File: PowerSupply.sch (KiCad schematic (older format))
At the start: 62 parts, among them J1 Conn_01x03, J2 Conn_01x02, J22 Jack-DC, J23 Conn_01x02, J24 Conn_01x02, J25 Conn_01x01, J26 Conn_01x01, J27 Conn_01x01, J28 Conn_01x01, J3 Conn_01x02, J6 Conn_01x01, J7 Conn_01x01, J8 Conn_01x01, J9 Conn_01x01, Q1 2N3904, Q2 TIP42C, U1 LM317, U2 LM337

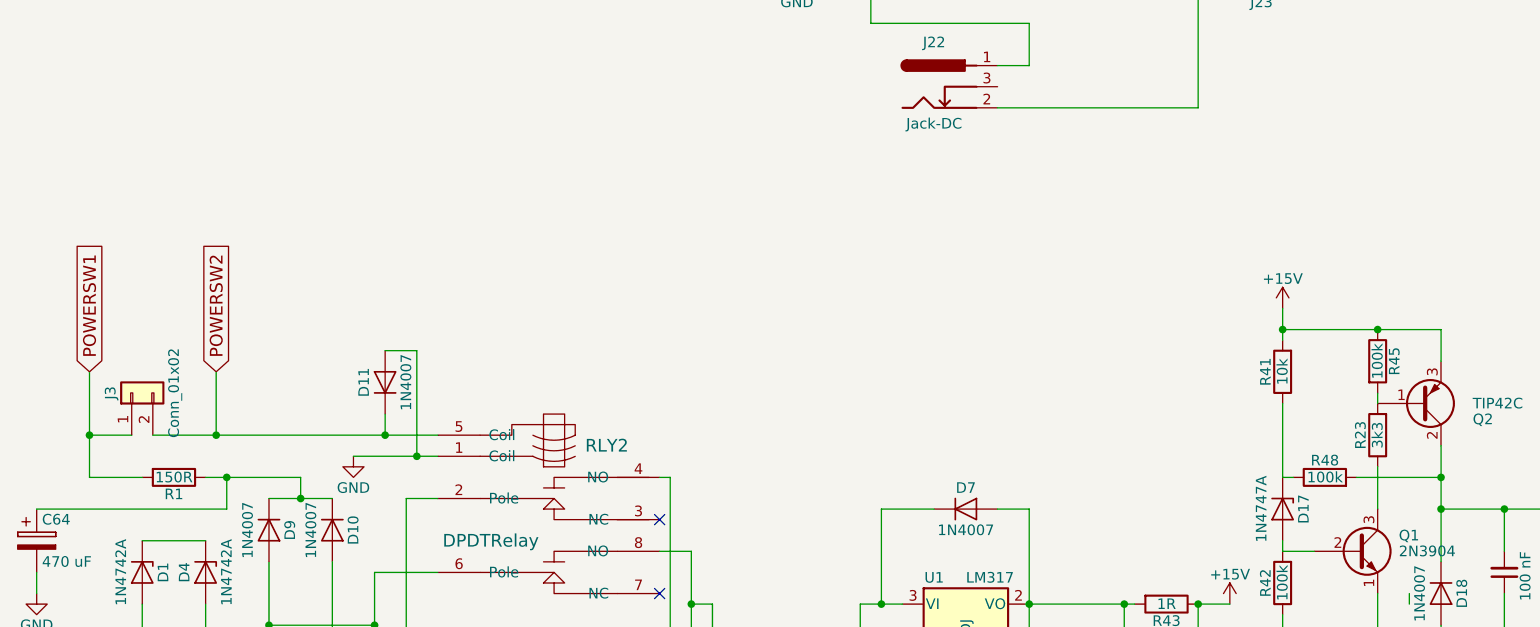
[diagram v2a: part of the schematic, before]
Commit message: Added jumpers to connect shields of XLR to ground
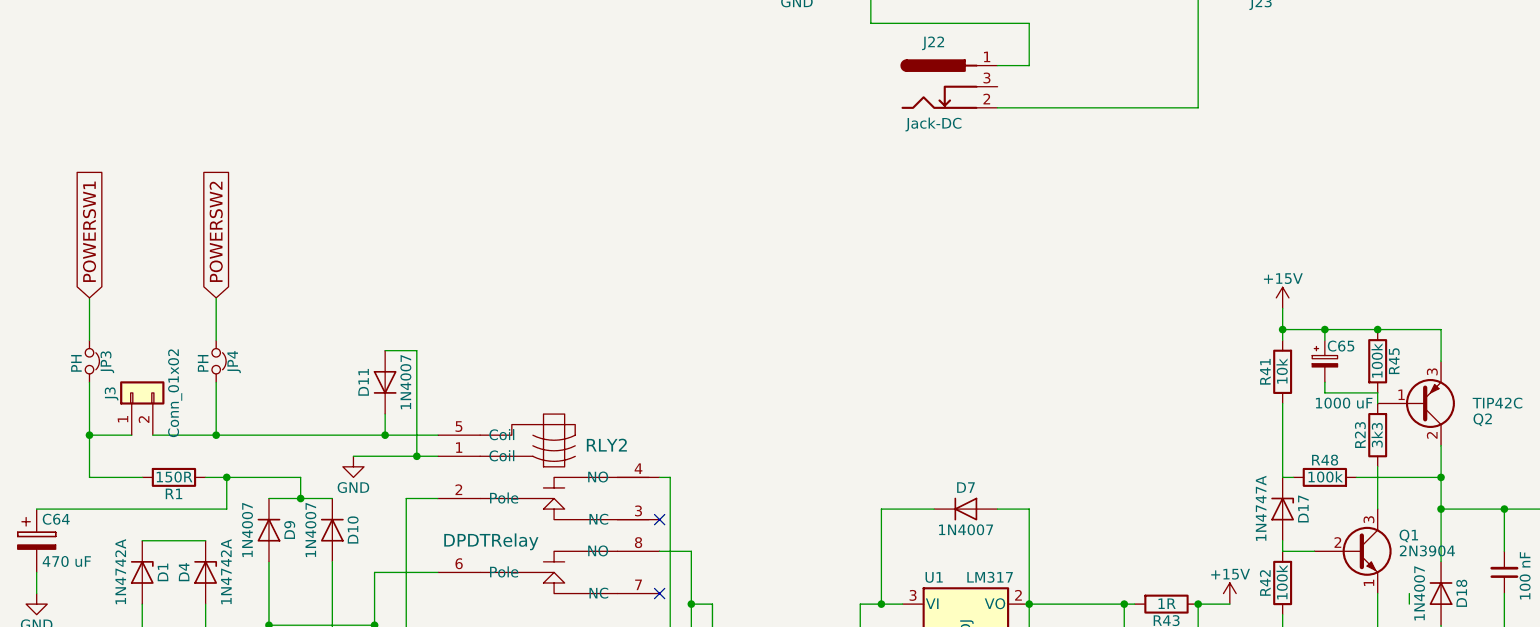
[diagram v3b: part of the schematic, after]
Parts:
- added C65: 1000 uF, Capacitors_THT:CP_Radial_D7.5mm_P2.50mm, symbol CP_Small
- added JP3, JP4: PH, Pin_Headers:Pin_Header_Straight_1x02_Pitch2.54mm, symbol Jumper_NC_Small
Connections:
- net +15V: now also C65.1
- net POWERSW1: now also JP3.1; no longer J3.1 (Pin_1), R1.2
- net POWERSW2: now also JP4.1; no longer D11.1 (K), J3.2 (Pin_2), RLY2.5 (Coil)
- net at Q2.1 (B), R23.2, R45.2: now also C65.2
- new net: D11.1 (K), J3.2 (Pin_2), JP4.2, RLY2.5 (Coil)
- new net: J3.1 (Pin_1), JP3.2, R1.2
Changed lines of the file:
@@
 $EndComp
 $Comp
-L GND #PWR81
+L GND #PWR83
 U 1 1 606D5FED
 P 1350 7050
-F 0 "#PWR81" H 1350 6800 50  0001 C CNN
+F 0 "#PWR83" H 1350 6800 50  0001 C CNN
 F 1 "GND" H 1350 6900 50  0000 C CNN
 F 2 "" H 1350 7050 50  0001 C CNN
@@
 $EndComp
 $Comp
-L GND #PWR82
+L GND #PWR84
 U 1 1 606D606A
 P 2150 4900
-F 0 "#PWR82" H 2150 4650 50  0001 C CNN
+F 0 "#PWR84" H 2150 4650 50  0001 C CNN
 F 1 "GND" H 2150 4750 50  0000 C CNN
 F 2 "" H 2150 4900 50  0001 C CNN
@@
 $EndComp
 $Comp
-L GND #PWR84
+L GND #PWR86
 U 1 1 606D6085
 P 4000 7200
-F 0 "#PWR84" H 4000 6950 50  0001 C CNN
+F 0 "#PWR86" H 4000 6950 50  0001 C CNN
 F 1 "GND" H 4000 7050 50  0000 C CNN
 F 2 "" H 4000 7200 50  0001 C CNN
@@
 NoConn ~ 3600 5200
 $Comp
-L GND #PWR89
+L GND #PWR91
 U 1 1 606D60BA
 P 6300 6300
-F 0 "#PWR89" H 6300 6050 50  0001 C CNN
+F 0 "#PWR91" H 6300 6050 50  0001 C CNN
 F 1 "GND" H 6300 6150 50  0000 C CNN
 F 2 "" H 6300 6300 50  0001 C CNN
@@
 	1    0    0    -1
 $EndComp
-Text GLabel 900  4500 1    60   Input ~ 0
+Text GLabel 900  4150 1    60   Input ~ 0
 POWERSW1
-Text GLabel 1500 4500 1    60   Input ~ 0
+Text GLabel 1500 4150 1    60   Input ~ 0
 POWERSW2
 $Comp
@@
 Power Supply
 $Comp
-L GND #PWR93
+L GND #PWR95
 U 1 1 606DF2B7
 P 7300 5750
-F 0 "#PWR93" H 7300 5500 50  0001 C CNN
+F 0 "#PWR95" H 7300 5500 50  0001 C CNN
 F 1 "GND" H 7300 5600 50  0000 C CNN
 F 2 "" H 7300 5750 50  0001 C CNN
@@
 SUBUNBAL
 $Comp
-L GND #PWR104
+L GND #PWR106
 U 1 1 606F678E
 P 10600 1400
-F 0 "#PWR104" H 10600 1150 50  0001 C CNN
+F 0 "#PWR106" H 10600 1150 50  0001 C CNN
 F 1 "GND" H 10600 1250 50  0000 C CNN
 F 2 "" H 10600 1400 50  0001 C CNN
@@
 $EndComp
 $Comp
-L GND #PWR105
+L GND #PWR107
 U 1 1 606F6A81
 P 10600 1750
-F 0 "#PWR105" H 10600 1500 50  0001 C CNN
+F 0 "#PWR107" H 10600 1500 50  0001 C CNN
 F 1 "GND" H 10600 1600 50  0000 C CNN
 F 2 "" H 10600 1750 50  0001 C CNN
@@
 $EndComp
 $Comp
-L GND #PWR97
+L GND #PWR99
 U 1 1 606F6F41
 P 9350 1100
-F 0 "#PWR97" H 9350 850 50  0001 C CNN
+F 0 "#PWR99" H 9350 850 50  0001 C CNN
 F 1 "GND" H 9350 950 50  0000 C CNN
 F 2 "" H 9350 1100 50  0001 C CNN
@@
 $EndComp
 $Comp
-L GND #PWR106
+L GND #PWR108
 U 1 1 606F7436
 P 10600 2450
-F 0 "#PWR106" H 10600 2200 50  0001 C CNN
+F 0 "#PWR108" H 10600 2200 50  0001 C CNN
 F 1 "GND" H 10600 2300 50  0000 C CNN
 F 2 "" H 10600 2450 50  0001 C CNN
@@
 $EndComp
 $Comp
-L GND #PWR107
+L GND #PWR109
 U 1 1 606F7669
 P 10600 2800
-F 0 "#PWR107" H 10600 2550 50  0001 C CNN
+F 0 "#PWR109" H 10600 2550 50  0001 C CNN
 F 1 "GND" H 10600 2650 50  0000 C CNN
 F 2 "" H 10600 2800 50  0001 C CNN
@@
 $EndComp
 $Comp
-L GND #PWR108
+L GND #PWR110
 U 1 1 606F84BF
 P 10600 3450
-F 0 "#PWR108" H 10600 3200 50  0001 C CNN
+F 0 "#PWR110" H 10600 3200 50  0001 C CNN
 F 1 "GND" H 10600 3300 50  0000 C CNN
 F 2 "" H 10600 3450 50  0001 C CNN
@@
 $EndComp
 $Comp
-L GND #PWR109
+L GND #PWR111
 U 1 1 606F8632
 P 10600 3800
-F 0 "#PWR109" H 10600 3550 50  0001 C CNN
+F 0 "#PWR111" H 10600 3550 50  0001 C CNN
 F 1 "GND" H 10600 3650 50  0000 C CNN
 F 2 "" H 10600 3800 50  0001 C CNN
@@
 $EndComp
 $Comp
-L GND #PWR100
+L GND #PWR102
 U 1 1 606F8F91
 P 10550 4450
-F 0 "#PWR100" H 10550 4200 50  0001 C CNN
+F 0 "#PWR102" H 10550 4200 50  0001 C CNN
 F 1 "GND" H 10550 4300 50  0000 C CNN
 F 2 "" H 10550 4450 50  0001 C CNN
@@
 $EndComp
 $Comp
-L GND #PWR101
+L GND #PWR103
 U 1 1 606F910C
 P 10550 4800
-F 0 "#PWR101" H 10550 4550 50  0001 C CNN
+F 0 "#PWR103" H 10550 4550 50  0001 C CNN
 F 1 "GND" H 10550 4650 50  0000 C CNN
 F 2 "" H 10550 4800 50  0001 C CNN
@@
 $EndComp
 $Comp
-L GND #PWR98
+L GND #PWR100
 U 1 1 606F9F16
 P 9350 2150
-F 0 "#PWR98" H 9350 1900 50  0001 C CNN
+F 0 "#PWR100" H 9350 1900 50  0001 C CNN
 F 1 "GND" H 9350 2000 50  0000 C CNN
 F 2 "" H 9350 2150 50  0001 C CNN
@@
 $EndComp
 $Comp
-L GND #PWR99
+L GND #PWR101
 U 1 1 606FA0A1
 P 9350 3150
-F 0 "#PWR99" H 9350 2900 50  0001 C CNN
+F 0 "#PWR101" H 9350 2900 50  0001 C CNN
 F 1 "GND" H 9350 3000 50  0000 C CNN
 F 2 "" H 9350 3150 50  0001 C CNN
@@
 $EndComp
 $Comp
-L GND #PWR96
+L GND #PWR98
 U 1 1 606FA305
 P 9300 4150
-F 0 "#PWR96" H 9300 3900 50  0001 C CNN
+F 0 "#PWR98" H 9300 3900 50  0001 C CNN
 F 1 "GND" H 9300 4000 50  0000 C CNN
 F 2 "" H 9300 4150 50  0001 C CNN
@@
 $EndComp
 $Comp
-L GND #PWR102
+L GND #PWR104
 U 1 1 606FAB7E
 P 10550 5450
-F 0 "#PWR102" H 10550 5200 50  0001 C CNN
+F 0 "#PWR104" H 10550 5200 50  0001 C CNN
 F 1 "GND" H 10550 5300 50  0000 C CNN
 F 2 "" H 10550 5450 50  0001 C CNN
@@
 $EndComp
 $Comp
-L GND #PWR103
+L GND #PWR105
 U 1 1 606FAD7D
 P 10550 5800
-F 0 "#PWR103" H 10550 5550 50  0001 C CNN
+F 0 "#PWR105" H 10550 5550 50  0001 C CNN
 F 1 "GND" H 10550 5650 50  0000 C CNN
 F 2 "" H 10550 5800 50  0001 C CNN
@@
 $EndComp
 $Comp
-L GND #PWR87
+L GND #PWR89
 U 1 1 606FCAFD
 P 4400 2050
-F 0 "#PWR87" H 4400 1800 50  0001 C CNN
+F 0 "#PWR89" H 4400 1800 50  0001 C CNN
 F 1 "GND" H 4400 1900 50  0000 C CNN
 F 2 "" H 4400 2050 50  0001 C CNN
@@
 $EndComp
 $Comp
-L +15V #PWR88
+L +15V #PWR90
 U 1 1 6070415B
 P 6300 5600
-F 0 "#PWR88" H 6300 5450 50  0001 C CNN
+F 0 "#PWR90" H 6300 5450 50  0001 C CNN
 F 1 "+15V" H 6300 5740 50  0000 C CNN
 F 2 "" H 6300 5600 50  0001 C CNN
@@
 $EndComp
 $Comp
-L -15V #PWR90
+L -15V #PWR92
 U 1 1 60704F1D
 P 6300 7000
-F 0 "#PWR90" H 6300 7100 50  0001 C CNN
+F 0 "#PWR92" H 6300 7100 50  0001 C CNN
 F 1 "-15V" H 6300 7150 50  0000 C CNN
 F 2 "" H 6300 7000 50  0001 C CNN
@@
 $EndComp
 $Comp
-L -15V #PWR92
+L -15V #PWR94
 U 1 1 607050A0
 P 6550 5850
-F 0 "#PWR92" H 6550 5950 50  0001 C CNN
+F 0 "#PWR94" H 6550 5950 50  0001 C CNN
 F 1 "-15V" H 6550 6000 50  0000 C CNN
 F 2 "" H 6550 5850 50  0001 C CNN
@@
 $EndComp
 $Comp
-L +15V #PWR91
+L +15V #PWR93
 U 1 1 60705366
 P 6550 4200
-F 0 "#PWR91" H 6550 4050 50  0001 C CNN
+F 0 "#PWR93" H 6550 4050 50  0001 C CNN
 F 1 "+15V" H 6550 4340 50  0000 C CNN
 F 2 "" H 6550 4200 50  0001 C CNN
@@
 $EndComp
 $Comp
-L +15V #PWR83
+L +15V #PWR85
 U 1 1 60705AF1
 P 3100 7150
-F 0 "#PWR83" H 3100 7000 50  0001 C CNN
+F 0 "#PWR85" H 3100 7000 50  0001 C CNN
 F 1 "+15V" H 3100 7290 50  0000 C CNN
 F 2 "" H 3100 7150 50  0001 C CNN
@@
 $EndComp
 $Comp
-L GND #PWR86
+L GND #PWR88
 U 1 1 60706D8C
 P 4250 2600
-F 0 "#PWR86" H 4250 2350 50  0001 C CNN
+F 0 "#PWR88" H 4250 2350 50  0001 C CNN
 F 1 "GND" H 4250 2450 50  0000 C CNN
 F 2 "" H 4250 2600 50  0001 C CNN
@@
 $EndComp
 $Comp
-L -15V #PWR85
+L -15V #PWR87
 U 1 1 607072F3
 P 4050 1850
-F 0 "#PWR85" H 4050 1950 50  0001 C CNN
+F 0 "#PWR87" H 4050 1950 50  0001 C CNN
 F 1 "-15V" H 4050 2000 50  0000 C CNN
 F 2 "" H 4050 1850 50  0001 C CNN
@@
 $EndComp
 $Comp
-L GND #PWR95
+L GND #PWR97
 U 1 1 6070A0C7
 P 8450 5250
-F 0 "#PWR95" H 8450 5000 50  0001 C CNN
+F 0 "#PWR97" H 8450 5000 50  0001 C CNN
 F 1 "GND" H 8450 5100 50  0000 C CNN
 F 2 "" H 8450 5250 50  0001 C CNN
@@
 $EndComp
 $Comp
-L GND #PWR94
+L GND #PWR96
 U 1 1 607B2586
 P 7600 5750
-F 0 "#PWR94" H 7600 5500 50  0001 C CNN
+F 0 "#PWR96" H 7600 5500 50  0001 C CNN
 F 1 "GND" H 7600 5600 50  0000 C CNN
 F 2 "" H 7600 5750 50  0001 C CNN
@@
 Connection ~ 4350 6250
 Wire Wire Line
-	1900 5000 1450 5000
+	1450 5000 1900 5000
 Wire Wire Line
 	900  5000 1150 5000
@@
 Connection ~ 900  4800
 Wire Wire Line
-	900  4500 900  5000
-Wire Wire Line
-	1500 4500 1500 4800
+	900  4550 900  5000
 Connection ~ 1500 4800
 Wire Wire Line
@@
 $EndComp
 $Comp
-L GND #PWR80
+L GND #PWR82
 U 1 1 60843522
 P 650 5550
-F 0 "#PWR80" H 650 5300 50  0001 C CNN
+F 0 "#PWR82" H 650 5300 50  0001 C CNN
 F 1 "GND" H 650 5400 50  0000 C CNN
 F 2 "" H 650 5550 50  0001 C CNN
@@
 	1550 5150 650  5150
 Connection ~ 1550 5000
+$Comp
+L CP_Small C65
+U 1 1 608C9A64
+P 6750 4450
+F 0 "C65" H 6760 4520 50  0000 L CNN
+F 1 "1000 uF" H 6700 4250 50  0000 L CNN
+F 2 "Capacitors_THT:CP_Radial_D7.5mm_P2.50mm" H 6750 4450 50  0001 C CNN
+F 3 "" H 6750 4450 50  0001 C CNN
+	1    6750 4450
+	1    0    0    -1
+$EndComp
+Wire Wire Line
+	7000 4600 6750 4600
+Wire Wire Line
+	6750 4600 6750 4550
+Wire Wire Line
+	6750 4350 6750 4300
+Connection ~ 6750 4300
+$Comp
+L Jumper_NC_Small JP3
+U 1 1 608E1F82
+P 900 4450
+F 0 "JP3" H 900 4530 50  0000 C CNN
+F 1 "PH" H 910 4390 50  0000 C CNN
+F 2 "Pin_Headers:Pin_Header_Straight_1x02_Pitch2.54mm" H 900 4450 50  0001 C CNN
+F 3 "" H 900 4450 50  0001 C CNN
+	1    900  4450
+	0    1    1    0
+$EndComp
+Wire Wire Line
+	900  4350 900  4150
+$Comp
+L Jumper_NC_Small JP4
+U 1 1 608E242B
+P 1500 4450
+F 0 "JP4" H 1500 4530 50  0000 C CNN
+F 1 "PH" H 1510 4390 50  0000 C CNN
+F 2 "Pin_Headers:Pin_Header_Straight_1x02_Pitch2.54mm" H 1500 4450 50  0001 C CNN
+F 3 "" H 1500 4450 50  0001 C CNN
+	1    1500 4450
+	0    1    1    0
+$EndComp
+Wire Wire Line
+	1500 4350 1500 4150
+Wire Wire Line
+	1500 4550 1500 4800
 $EndSCHEMATC
